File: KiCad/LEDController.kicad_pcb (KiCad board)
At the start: 4 copper layers, 50 x 50 mm, 46 parts, among them J1 UART, J2 VDD, J3 GND, J4 Conn_01x05, J5 Conn_01x03, J6 USB_C_Receptacle_USB2.0_16P, J7 Conn_01x14, J8 JTAG, Q1 IRLZ44N, Q2 IRLZ44N, Q3 IRLZ44N, Q4 IRLZ44N, SW1 BOOT, SW2 EN, U1 TPS54202DDC, U2 ESP32-S3-WROOM-2

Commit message: jlcpcb order
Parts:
- added C12: 10u, Capacitor_SMD:C_0805_2012Metric_Pad1.18x1.45mm_HandSolder, F.Cu at (106.2, 56.1)
- C4: value 22u -> 10u
- moved C4 2.06 mm to (104.1, 56.1)
- moved C2 1.55 mm to (101.1, 55.5), turned to 90 degrees
- moved D1 0.89 mm to (102.6, 74.3)
- moved C5 0.76 mm to (102.6, 59.2)
- moved J1 0.51 mm to (106.7, 51.3)
- moved R8 0.38 mm to (106.7, 74.3)
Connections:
- U2 pad 25: GPIO.48 -> unconnected-(U2-GPIO48/SPICLK_N/SUBSPICLK_N_DIFF-Pad25)
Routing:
- net GPIO.17: track 26.0 -> 23.8 mm
- net GPIO.13: track 16.3 -> 14.1 mm
- net GPIO.38: track 24.7 -> 22.5 mm
- net GPIO.47: track 28.7 -> 26.6 mm
- net GPIO.8: track 28.4 -> 26.2 mm
- net GPIO.46: track 27.7 -> 25.6 mm
- net GPIO.11: track 23.9 -> 21.7 mm
- net GPIO.12: track 19.0 -> 16.9 mm
- net GPIO.18: track 25.9 -> 23.9 mm
- net GPIO.14: track 14.7 -> 13.1 mm
- net GPIO.21: track 14.0 -> 12.5 mm
- net +24V: track 80.3 -> 79.5 mm
- net Net-(D1-A): track 1.68 -> 2.19 mm
- net GND: vias 21 -> 33
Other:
- board text added: "3V3"
- board text added: "CK"
- board text added: "DATA"
- board text added: "DI"
- board text added: "DO"
- board text added: "G11"
- board text added: "G12"
- board text added: "G13"
- board text added: "G14"
- board text added: "G17"
- board text added: "G18"
- board text added: "G21"
- board text added: "G38"
- board text added: "G45"
- board text added: "G46"
- board text added: "G47"
- board text added: "G8"
- board text added: "MS"

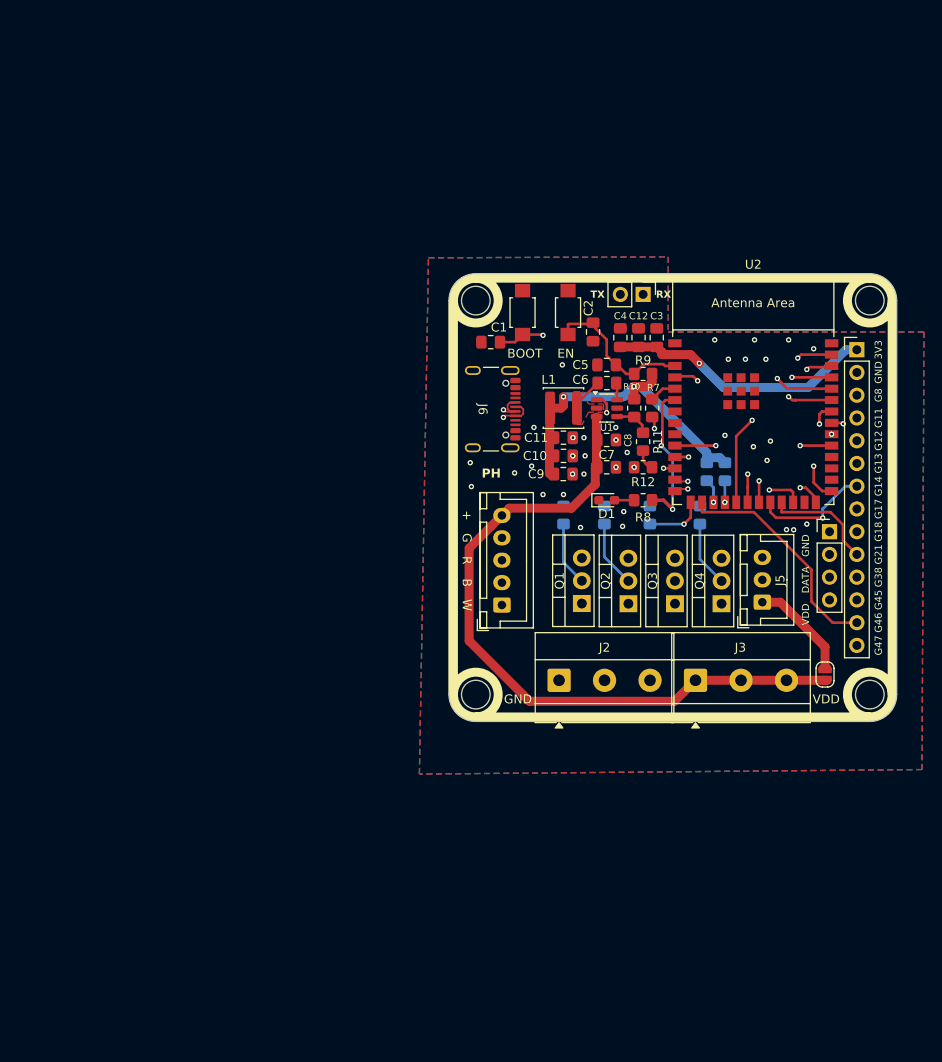
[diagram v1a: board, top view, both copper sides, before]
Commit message: add 5v buck converter
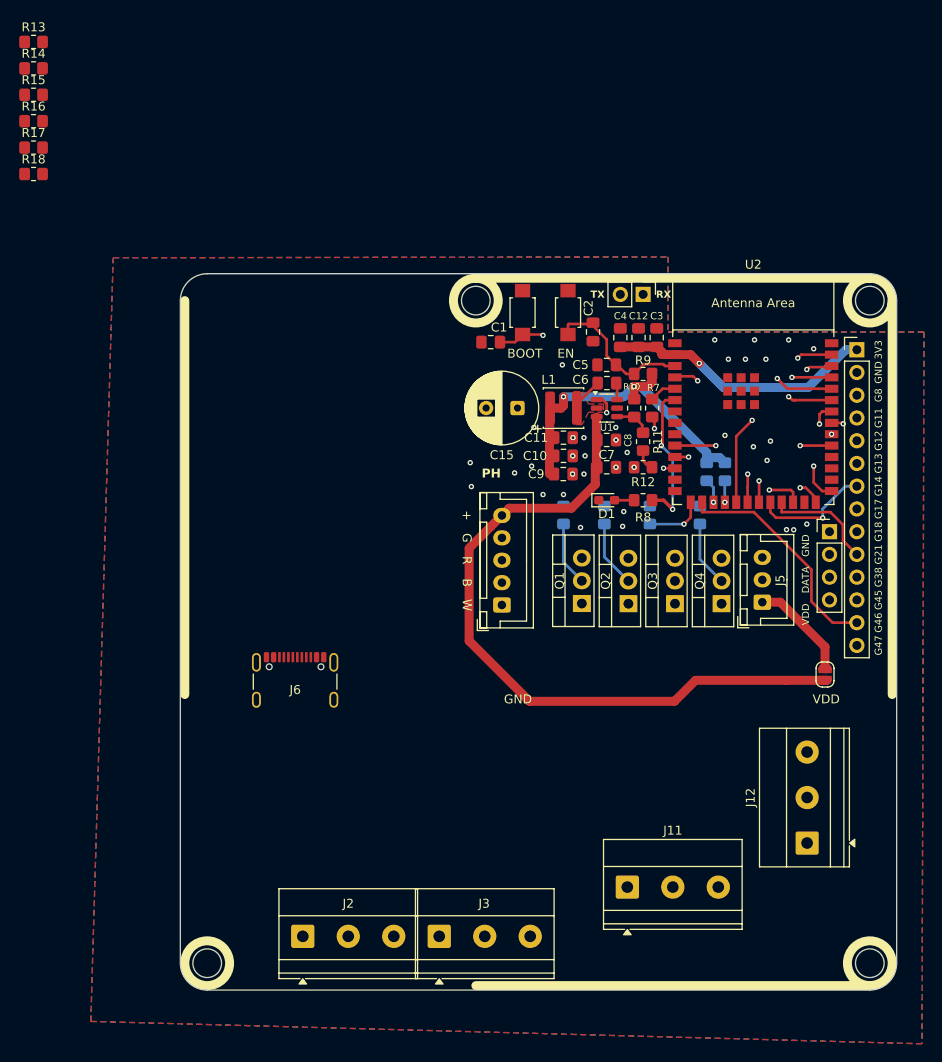
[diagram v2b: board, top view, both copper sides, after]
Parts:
- added C15: 220uF, Capacitor_THT:CP_Radial_D8.0mm_P3.50mm, F.Cu at (92.7, 64.0)
- added J11: LED_Data, TerminalBlock_Phoenix:TerminalBlock_Phoenix_MKDS-1,5-3-5.08_1x03_P5.08mm_Horizontal, F.Cu at (104.9, 117.5)
- added J12: LED_Data, TerminalBlock_Phoenix:TerminalBlock_Phoenix_MKDS-1,5-3-5.08_1x03_P5.08mm_Horizontal, F.Cu at (125.0, 112.6)
- added R13: 100, Resistor_SMD:R_0805_2012Metric_Pad1.20x1.40mm_HandSolder, F.Cu at (38.6, 23.1)
- added R14: 100, Resistor_SMD:R_0805_2012Metric_Pad1.20x1.40mm_HandSolder, F.Cu at (38.6, 26.1)
- added R15: 100, Resistor_SMD:R_0805_2012Metric_Pad1.20x1.40mm_HandSolder, F.Cu at (38.6, 29.0)
- added R16: 100, Resistor_SMD:R_0805_2012Metric_Pad1.20x1.40mm_HandSolder, F.Cu at (38.6, 32.0)
- added R17: 100, Resistor_SMD:R_0805_2012Metric_Pad1.20x1.40mm_HandSolder, F.Cu at (38.6, 34.9)
- added R18: 100, Resistor_SMD:R_0805_2012Metric_Pad1.20x1.40mm_HandSolder, F.Cu at (38.6, 37.9)
- L1: value 15u -> 10u
- moved H4 42.4 mm to (58.0, 126.0)
- moved J2 40.5 mm to (68.7, 123.0)
- moved J3 40.5 mm to (83.9, 123.0)
- moved J6 37.7 mm to (67.8, 95.5), turned to 0 degrees
- moved H3 30.0 mm to (132.0, 126.0)
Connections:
- J7 pad 4: GPIO.11 -> unconnected-(J7-Pin_4-Pad4)
- J7 pad 5: GPIO.12 -> unconnected-(J7-Pin_5-Pad5)
- J7 pad 6: GPIO.13 -> unconnected-(J7-Pin_6-Pad6)
- J7 pad 7: GPIO.14 -> unconnected-(J7-Pin_7-Pad7)
- J7 pad 8: GPIO.17 -> unconnected-(J7-Pin_8-Pad8)
- J7 pad 9: GPIO.18 -> unconnected-(J7-Pin_9-Pad9)
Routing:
- net USB.D+: track 33.3 -> 0.00 mm, vias 2 -> 0
- net USB.D-: track 33.2 -> 0.00 mm, vias 2 -> 0
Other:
- board size 50 x 50 mm -> 80 x 80 mm

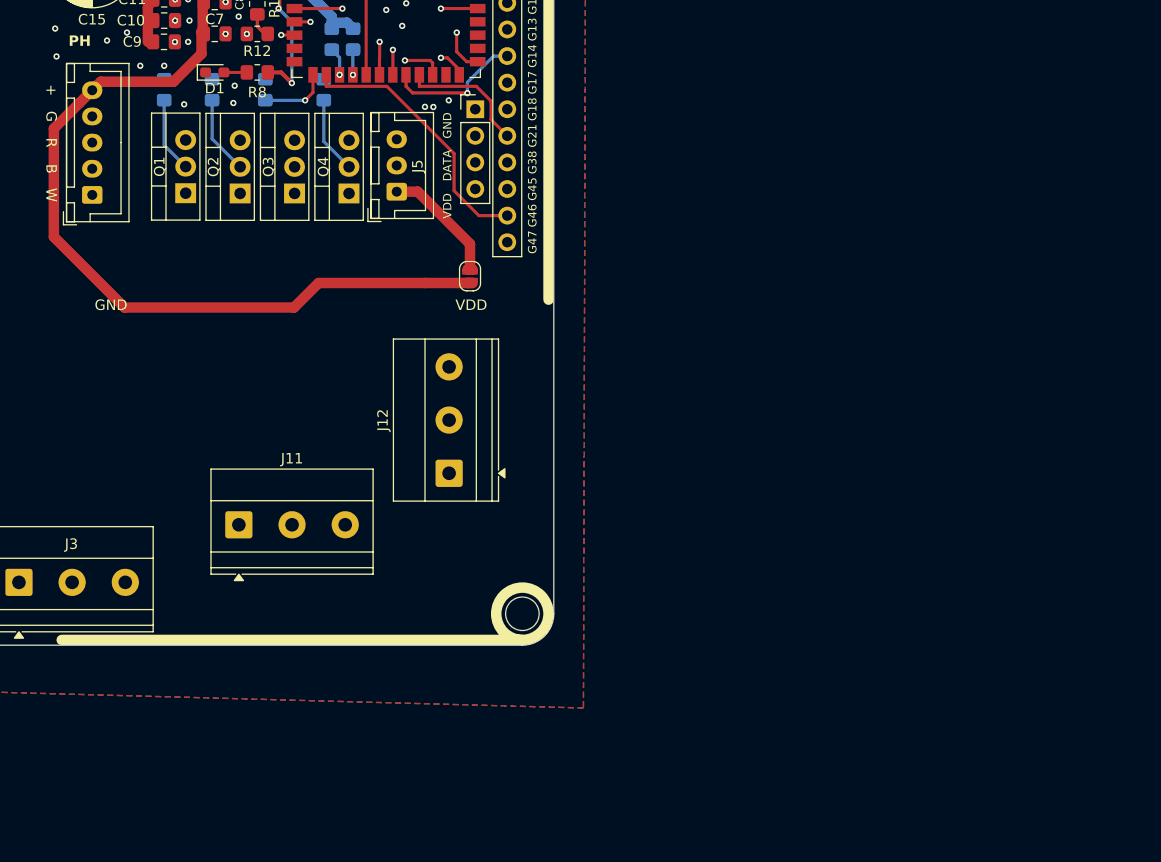
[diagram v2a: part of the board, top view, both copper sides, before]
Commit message: delete pwm, add 12 neopixel outputs
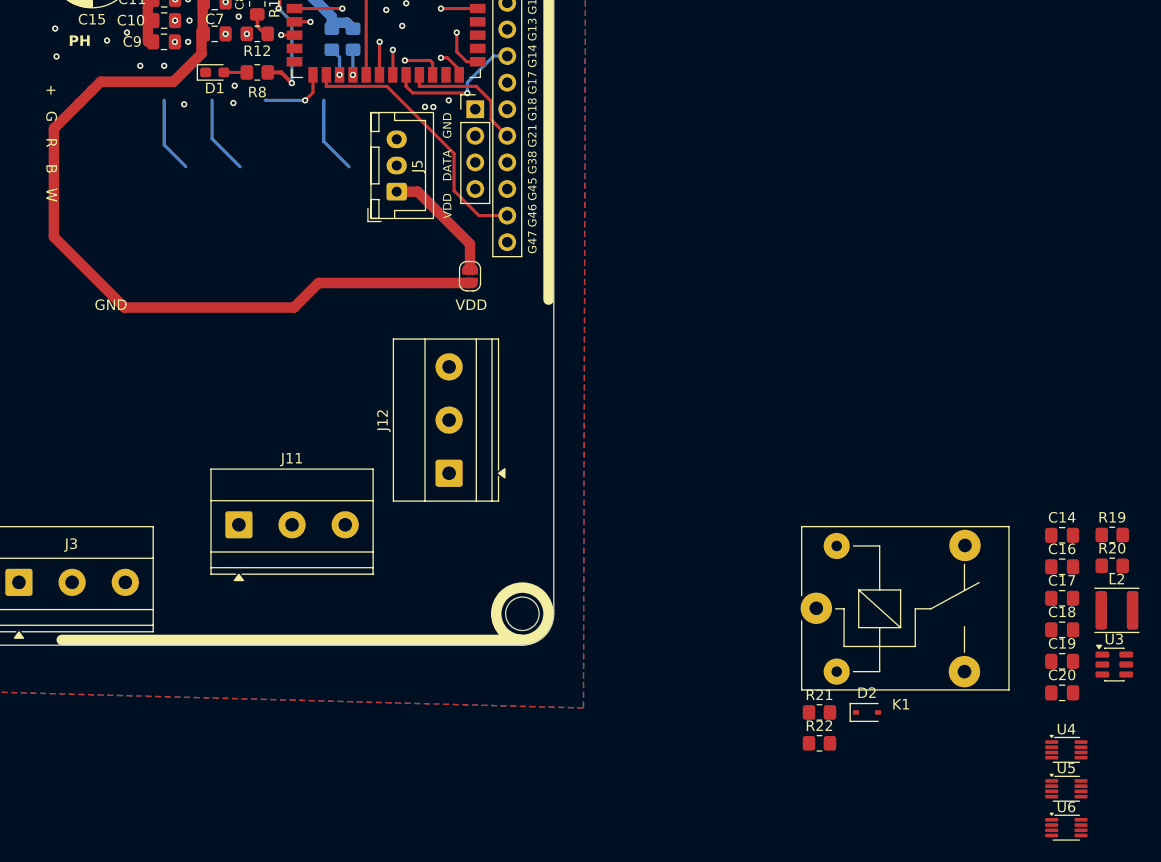
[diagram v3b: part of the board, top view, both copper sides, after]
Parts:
- removed J4: Conn_01x05, Connector_JST:JST_XH_B5B-XH-A_1x05_P2.50mm_Vertical
- removed Q1, Q2, Q3, Q4: IRLZ44N, Package_TO_SOT_THT:TO-220-3_Vertical
- removed R1, R2, R3, R4: 100k, Resistor_SMD:R_0805_2012Metric_Pad1.20x1.40mm_HandSolder
- added C14: 100n, Capacitor_SMD:C_0805_2012Metric_Pad1.18x1.45mm_HandSolder, F.Cu at (183.6, 118.5)
- added C16: 100n, Capacitor_SMD:C_0805_2012Metric_Pad1.18x1.45mm_HandSolder, F.Cu at (183.6, 121.5)
- added C17: 10u, Capacitor_SMD:C_0805_2012Metric_Pad1.18x1.45mm_HandSolder, F.Cu at (183.6, 124.5)
- added C18: 10u, Capacitor_SMD:C_0805_2012Metric_Pad1.18x1.45mm_HandSolder, F.Cu at (183.6, 127.5)
- added C19: 10u, Capacitor_SMD:C_0805_2012Metric_Pad1.18x1.45mm_HandSolder, F.Cu at (183.6, 130.5)
- added C20: 10u, Capacitor_SMD:C_0805_2012Metric_Pad1.18x1.45mm_HandSolder, F.Cu at (183.6, 133.6)
- added D2: 1N4148WS, Diode_SMD:D_SOD-323, F.Cu at (164.9, 135.4)
- added K1: SRD-05VDC-SL-C, Relay_THT:Relay_SPDT_SANYOU_SRD_Series_Form_C, F.Cu at (160.1, 125.5)
- added L2: 15u, Inductor_SMD:L_APV_ANR4026, F.Cu at (188.8, 125.7)
- added R19: 100k, Resistor_SMD:R_0805_2012Metric_Pad1.20x1.40mm_HandSolder, F.Cu at (188.3, 118.5)
- added R20: 13.3k, Resistor_SMD:R_0805_2012Metric_Pad1.20x1.40mm_HandSolder, F.Cu at (188.3, 121.4)
- added R21: 100k, Resistor_SMD:R_0805_2012Metric_Pad1.20x1.40mm_HandSolder, F.Cu at (160.4, 135.4)
- added R22: 100, Resistor_SMD:R_0805_2012Metric_Pad1.20x1.40mm_HandSolder, F.Cu at (160.4, 138.4)
- added U3: TPS54202DDC, Package_TO_SOT_SMD:SOT-23-6, F.Cu at (188.5, 130.8)
- added U4: SN74LVC2T45DCUR, Package_SO:VSSOP-8_2.3x2mm_P0.5mm, F.Cu at (184.0, 139.0)
- added U5: SN74LVC2T45DCUR, Package_SO:VSSOP-8_2.3x2mm_P0.5mm, F.Cu at (184.0, 142.7)
- added U6: SN74LVC2T45DCUR, Package_SO:VSSOP-8_2.3x2mm_P0.5mm, F.Cu at (184.0, 146.4)
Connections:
- R13 pad 2: GPIO.11 -> Net-(U4-B1)
- R14 pad 2: GPIO.12 -> Net-(U4-B2)
- R15 pad 1: GPIO.13 -> Net-(U5-B1)
- R16 pad 2: GPIO.14 -> Net-(U5-B2)
- R17 pad 2: GPIO.17 -> Net-(U6-B1)
- R18 pad 1: GPIO.18 -> Net-(U6-B2)
- U2 pad 6: GPIO.6 -> Relay_drive
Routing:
- net (no net): track 0.00 -> 82.9 mm
- net W_out: track 27.8 -> 0.00 mm
- net B_out: track 22.6 -> 0.00 mm
- net G_out: track 21.5 -> 0.00 mm
- net R_out: track 10.9 -> 0.00 mm

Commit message: work on new design
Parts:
- removed J11, J12: LED_Data, TerminalBlock_Phoenix:TerminalBlock_Phoenix_MKDS-1,5-3-5.08_1x03_P5.08mm_Horizontal
- removed J5: Conn_01x03, Connector_JST:JST_XH_B3B-XH-A_1x03_P2.50mm_Vertical
- removed JP1: SolderJumper_2_Open, Jumper:SolderJumper-2_P1.3mm_Open_RoundedPad1.0x1.5mm
- removed R13, R14, R15, R16, R17, R18, R7: 100, Resistor_SMD:R_0805_2012Metric_Pad1.20x1.40mm_HandSolder
- removed U4, U5, U6: SN74LVC2T45DCUR, Package_SO:VSSOP-8_2.3x2mm_P0.5mm
- added C21: 220uF, Capacitor_THT:CP_Radial_D8.0mm_P3.50mm, F.Cu at (96.5, 89.2)
- added F1: Fuse, Fuse:Fuseholder_Blade_Mini_Keystone_3568, F.Cu at (127.3, 114.0)
- added J10: LED2, TerminalBlock_Phoenix:TerminalBlock_Phoenix_MKDS-3-3-5.08_1x03_P5.08mm_Horizontal, F.Cu at (167.0, 34.0)
- added J13: LED3, TerminalBlock_Phoenix:TerminalBlock_Phoenix_MKDS-3-3-5.08_1x03_P5.08mm_Horizontal, F.Cu at (59.8, 58.4)
- added J14: LED4, TerminalBlock_Phoenix:TerminalBlock_Phoenix_MKDS-3-3-5.08_1x03_P5.08mm_Horizontal, F.Cu at (184.3, 20.5)
- added J15: LED8, TerminalBlock_Phoenix:TerminalBlock_Phoenix_MKDS-3-3-5.08_1x03_P5.08mm_Horizontal, F.Cu at (184.3, 34.0)
- added J16: LED7, TerminalBlock_Phoenix:TerminalBlock_Phoenix_MKDS-3-3-5.08_1x03_P5.08mm_Horizontal, F.Cu at (59.8, 75.7)
- added J17: LED6, TerminalBlock_Phoenix:TerminalBlock_Phoenix_MKDS-3-3-5.08_1x03_P5.08mm_Horizontal, F.Cu at (201.6, 20.5)
- added J18: LED5, TerminalBlock_Phoenix:TerminalBlock_Phoenix_MKDS-3-3-5.08_1x03_P5.08mm_Horizontal, F.Cu at (201.6, 34.0)
- added J19: LED9, TerminalBlock_Phoenix:TerminalBlock_Phoenix_MKDS-3-3-5.08_1x03_P5.08mm_Horizontal, F.Cu at (59.8, 93.0)
- added J20: LED10, TerminalBlock_Phoenix:TerminalBlock_Phoenix_MKDS-3-3-5.08_1x03_P5.08mm_Horizontal, F.Cu at (218.9, 20.5)
- added J21: LED11, TerminalBlock_Phoenix:TerminalBlock_Phoenix_MKDS-3-3-5.08_1x03_P5.08mm_Horizontal, F.Cu at (218.9, 34.0)
- added J22: LED12, TerminalBlock_Phoenix:TerminalBlock_Phoenix_MKDS-3-3-5.08_1x03_P5.08mm_Horizontal, F.Cu at (59.8, 110.3)
- added J9: LED1, TerminalBlock_Phoenix:TerminalBlock_Phoenix_MKDS-3-3-5.08_1x03_P5.08mm_Horizontal, F.Cu at (167.0, 20.5)
- added Q5: AO3400A, Package_TO_SOT_SMD:SOT-23, F.Cu at (78.0, 93.2)
- added R35: 100, Resistor_SMD:R_0805_2012Metric_Pad1.20x1.40mm_HandSolder, F.Cu at (193.4, 67.0)
- added R36: 100, Resistor_SMD:R_0805_2012Metric_Pad1.20x1.40mm_HandSolder, F.Cu at (193.4, 70.0)
- added R37: 100, Resistor_SMD:R_0805_2012Metric_Pad1.20x1.40mm_HandSolder, F.Cu at (193.4, 72.9)
- added R38: 100, Resistor_SMD:R_0805_2012Metric_Pad1.20x1.40mm_HandSolder, F.Cu at (193.4, 75.9)
- added R39: 100, Resistor_SMD:R_0805_2012Metric_Pad1.20x1.40mm_HandSolder, F.Cu at (193.4, 78.8)
- added R40: 100, Resistor_SMD:R_0805_2012Metric_Pad1.20x1.40mm_HandSolder, F.Cu at (193.4, 81.8)
- added R41: 100, Resistor_SMD:R_0805_2012Metric_Pad1.20x1.40mm_HandSolder, F.Cu at (198.1, 67.0)
- added R42: 100, Resistor_SMD:R_0805_2012Metric_Pad1.20x1.40mm_HandSolder, F.Cu at (198.1, 70.0)
- added R43: 100, Resistor_SMD:R_0805_2012Metric_Pad1.20x1.40mm_HandSolder, F.Cu at (198.1, 72.9)
- added R44: 100, Resistor_SMD:R_0805_2012Metric_Pad1.20x1.40mm_HandSolder, F.Cu at (198.1, 75.9)
- added R45: 100, Resistor_SMD:R_0805_2012Metric_Pad1.20x1.40mm_HandSolder, F.Cu at (198.1, 78.8)
- added R46: 100, Resistor_SMD:R_0805_2012Metric_Pad1.20x1.40mm_HandSolder, F.Cu at (198.1, 81.8)
- added U7: SN74LVC8T245, Package_SO:TSSOP-24_4.4x7.8mm_P0.65mm, F.Cu at (205.2, 70.2)
- added U8: SN74LVC8T245, Package_SO:TSSOP-24_4.4x7.8mm_P0.65mm, F.Cu at (214.4, 70.2)
- L2: footprint Inductor_SMD:L_APV_ANR4026 -> Inductor_SMD:L_APV_APH0420
- moved H2 117.6 mm to (37.5, 121.9)
- moved L2 103.8 mm to (97.5, 76.2), turned to 180 degrees
- moved U3 101.8 mm to (102.6, 76.2)
- moved C20 101.5 mm to (97.5, 79.8)
- moved C19 98.9 mm to (97.5, 81.8)
- moved C18 96.5 mm to (97.5, 83.8)
- moved R19 92.9 mm to (105.7, 76.2), turned to -90 degrees
- moved C14 92.7 mm to (102.6, 73.4)
- moved C17 92.5 mm to (102.6, 79.8)
- moved R20 92.5 mm to (105.7, 80.0), turned to -90 degrees
- moved D2 91.3 mm to (84.0, 93.2), turned to 180 degrees
- moved R21 91.0 mm to (78.0, 96.7)
- moved C16 89.7 mm to (102.6, 82.8)
- moved R22 87.0 mm to (84.0, 96.7)
- moved K1 86.7 mm to (81.8, 88.3), turned to 90 degrees
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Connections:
- J2 pad 1: GND -> +24V
- J2 pad 2: GND -> +24V
- J2 pad 3: GND -> +24V
- J3 pad 1: +24V -> GND
- J3 pad 2: +24V -> GND
- J3 pad 3: +24V -> GND
- J7 pad 3: GPIO.8 -> unconnected-(J7-Pin_3-Pad3)
- K1 pad 1: +24V -> Net-(F1-Pad2)
- U2 pad 10: GPIO.17 -> Data12
- U2 pad 12: GPIO.8 -> Data5
- U2 pad 15: B -> I^{2}C.SCL
- U2 pad 17: I^{2}C.SDA -> Data6
- U2 pad 18: I^{2}C.SCL -> Data7
- U2 pad 19: GPIO.11 -> Data8
- U2 pad 20: GPIO.12 -> Data9
- U2 pad 21: GPIO.13 -> Data10
- U2 pad 22: GPIO.14 -> Data11
- U2 pad 38: G -> I^{2}C.SDA
- U2 pad 39: R -> Relay_drive
- U2 pad 4: W -> Data1
- U2 pad 5: Data -> Data2
- U2 pad 6: Relay_drive -> Data3
- U2 pad 7: unconnected-(U2-GPIO7/TOUCH7/ADC1_CH6-Pad7) -> Data4
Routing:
- net +24V: track 79.5 -> 12.1 mm
- net R: track 56.0 -> 0.00 mm, vias 2 -> 0
- net G: track 49.8 -> 0.00 mm, vias 2 -> 0
- net (no net): track 82.9 -> 33.6 mm, vias 0 -> 1
- net Net-(J5-Pin_2): track 35.2 -> 0.00 mm, vias 1 -> 0
- net W: track 33.6 -> 0.00 mm, vias 1 -> 0
- net Data1: track 0.00 -> 26.3 mm, vias 0 -> 1
- net GPIO.8: track 26.2 -> 0.00 mm, vias 1 -> 0
- net unconnected-(J7-Pin_8-Pad8): track 0.00 -> 23.8 mm, vias 0 -> 1
- net GPIO.17: track 23.8 -> 0.00 mm, vias 1 -> 0
- net Relay_drive: track 0.00 -> 23.6 mm, vias 0 -> 2
- net unconnected-(J7-Pin_4-Pad4): track 0.00 -> 21.7 mm, vias 0 -> 1
- net GPIO.11: track 21.7 -> 0.00 mm, vias 1 -> 0
- net I^{2}C.SDA: track 2.71 -> 24.2 mm, vias 1 -> 3
- net unconnected-(J7-Pin_5-Pad5): track 0.00 -> 16.9 mm, vias 0 -> 1
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- added copper zone on F.Cu, net Net-(U3-SW)
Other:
- board text removed: "+"
- board text removed: "+5-24V"
- board text removed: "B"
- board text removed: "G"
- board text removed: "R"
- board text removed: "W"

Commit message: work
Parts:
- moved J18 161.6 mm to (67.1, 123.4)
- moved J17 157.6 mm to (82.3, 123.4)
- moved J22 153.5 mm to (184.3, 20.5), turned to 0 degrees
- moved J14 151.5 mm to (59.8, 106.8), turned to -90 degrees
- moved J19 129.4 mm to (167.0, 20.5), turned to 0 degrees
- moved J10 115.3 mm to (59.8, 76.3), turned to -90 degrees
- moved J9 114.6 mm to (59.8, 61.1), turned to -90 degrees
- moved J15 114.6 mm to (112.8, 123.4)
- moved J2 113.8 mm to (182.1, 113.5)
- moved J3 113.8 mm to (197.4, 113.5)
- moved J16 60.8 mm to (97.5, 123.4), turned to 0 degrees
- moved J13 33.1 mm to (59.8, 91.5)
- moved J21 9.45 mm to (219.0, 43.4)
